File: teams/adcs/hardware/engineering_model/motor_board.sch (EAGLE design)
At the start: 63 parts

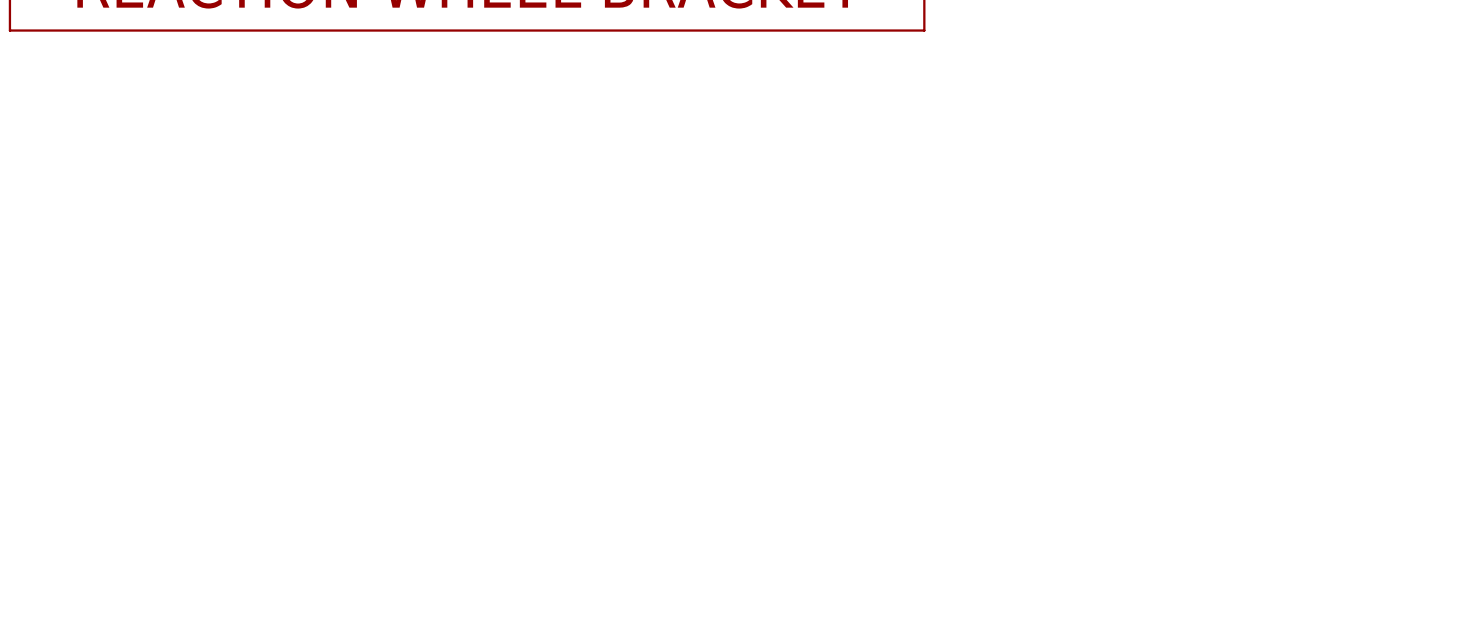
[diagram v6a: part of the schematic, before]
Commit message: ADCS/RW: Added LDOs for microcontrollers
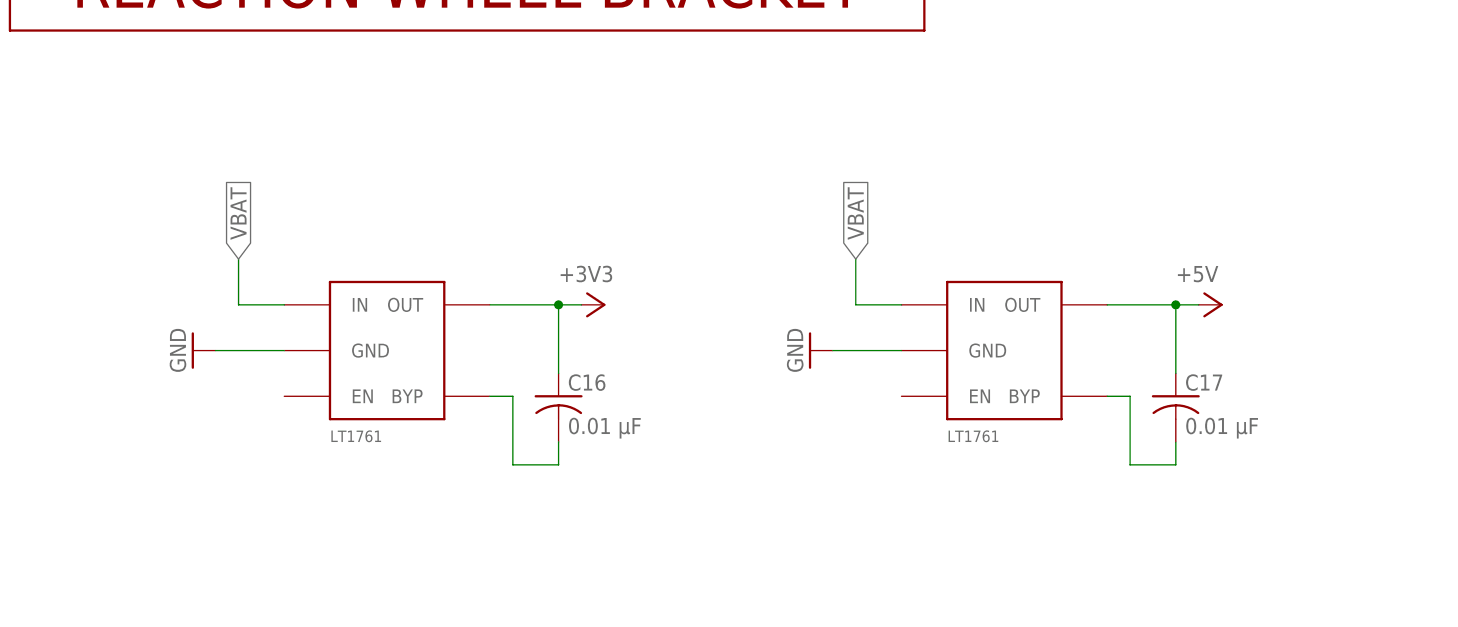
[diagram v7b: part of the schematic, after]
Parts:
- added C16, C17: 0.01 μF, rcl:C-USC0805
- added LDO_3V3, LDO_5V: LINEAR_LDO_LT1761-X, DubSat1 Components:LINEAR_LDO_LT1761-X
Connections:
- new net N$13: C17.2, LDO_5V.BYP
- new net N$14: C16.2, LDO_3V3.BYP
- net +3V3: now also C16.1, LDO_3V3.OUT
- net +5V: now also C17.1, LDO_5V.OUT
- net GND: now also LDO_3V3.GND, LDO_5V.GND
- net VBAT: now also LDO_3V3.IN, LDO_5V.IN
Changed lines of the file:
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@@
 <part name="SERIAL_X" library="SparkFun-Connectors" deviceset="CONN_03" device="LOCK"/>
 <part name="GND37" library="supply1" library_urn="urn:adsk.eagle:library:371" deviceset="GND" device=""/>
+<part name="LDO_3V3" library="DubSat1 Components" deviceset="LINEAR_LDO_LT1761-X" device=""/>
+<part name="LDO_5V" library="DubSat1 Components" deviceset="LINEAR_LDO_LT1761-X" device=""/>
+<part name="GND38" library="supply1" library_urn="urn:adsk.eagle:library:371" deviceset="GND" device=""/>
+<part name="GND39" library="supply1" library_urn="urn:adsk.eagle:library:371" deviceset="GND" device=""/>
+<part name="+3V4" library="supply1" library_urn="urn:adsk.eagle:library:371" deviceset="+3V3" device=""/>
+<part name="P+4" library="supply1" library_urn="urn:adsk.eagle:library:371" deviceset="+5V" device=""/>
+<part name="C16" library="rcl" library_urn="urn:adsk.eagle:library:334" deviceset="C-US" device="C0805" package3d_urn="urn:adsk.eagle:package:23617/2" value="0.01 μF"/>
+<part name="C17" library="rcl" library_urn="urn:adsk.eagle:library:334" deviceset="C-US" device="C0805" package3d_urn="urn:adsk.eagle:package:23617/2" value="0.01 μF"/>
 </parts>
 <sheets>
@@
 <instance part="SERIAL_X" gate="J$1" x="17.78" y="-129.54"/>
 <instance part="GND37" gate="1" x="35.56" y="-124.46" rot="R90"/>
+<instance part="LDO_3V3" gate="G$1" x="147.32" y="30.48"/>
+<instance part="LDO_5V" gate="G$1" x="215.9" y="30.48"/>
+<instance part="GND38" gate="1" x="193.04" y="30.48" rot="R270"/>
+<instance part="GND39" gate="1" x="124.46" y="30.48" rot="R270"/>
+<instance part="+3V4" gate="G$1" x="170.18" y="35.56" rot="R270"/>
+<instance part="P+4" gate="1" x="238.76" y="35.56" rot="R270"/>
+<instance part="C16" gate="G$1" x="165.1" y="25.4"/>
+<instance part="C17" gate="G$1" x="233.68" y="25.4"/>
 </instances>
 <busses>
@@
 <pinref part="GND37" gate="1" pin="GND"/>
 </segment>
+<segment>
+<pinref part="GND39" gate="1" pin="GND"/>
+<pinref part="LDO_3V3" gate="G$1" pin="GND"/>
+<wire x1="127" y1="30.48" x2="134.62" y2="30.48" width="0.1524" layer="91"/>
+</segment>
+<segment>
+<pinref part="GND38" gate="1" pin="GND"/>
+<pinref part="LDO_5V" gate="G$1" pin="GND"/>
+<wire x1="195.58" y1="30.48" x2="203.2" y2="30.48" width="0.1524" layer="91"/>
+</segment>
 </net>
 <net name="CANH" class="0">
@@
 <wire x1="38.1" y1="25.4" x2="33.02" y2="25.4" width="0.1524" layer="91"/>
 <label x="33.02" y="25.4" size="1.778" layer="95" rot="R180" xref="yes"/>
+</segment>
+<segment>
+<pinref part="LDO_3V3" gate="G$1" pin="IN"/>
+<wire x1="134.62" y1="35.56" x2="129.54" y2="35.56" width="0.1524" layer="91"/>
+<wire x1="129.54" y1="35.56" x2="129.54" y2="40.64" width="0.1524" layer="91"/>
+<label x="129.54" y="40.64" size="1.778" layer="95" rot="R90" xref="yes"/>
+</segment>
+<segment>
+<pinref part="LDO_5V" gate="G$1" pin="IN"/>
+<wire x1="203.2" y1="35.56" x2="198.12" y2="35.56" width="0.1524" layer="91"/>
+<wire x1="198.12" y1="35.56" x2="198.12" y2="40.64" width="0.1524" layer="91"/>
+<label x="198.12" y="40.64" size="1.778" layer="95" rot="R90" xref="yes"/>
 </segment>
 </net>
@@
 <junction x="261.62" y="-45.72"/>
 </segment>
+<segment>
+<pinref part="LDO_3V3" gate="G$1" pin="OUT"/>
+<pinref part="+3V4" gate="G$1" pin="+3V3"/>
+<wire x1="157.48" y1="35.56" x2="165.1" y2="35.56" width="0.1524" layer="91"/>
+<pinref part="C16" gate="G$1" pin="1"/>
+<wire x1="165.1" y1="35.56" x2="167.64" y2="35.56" width="0.1524" layer="91"/>
+<wire x1="165.1" y1="27.94" x2="165.1" y2="35.56" width="0.1524" layer="91"/>
+<junction x="165.1" y="35.56"/>
+</segment>
 </net>
 <net name="+5V" class="0">
@@
 <pinref part="P+3" gate="1" pin="+5V"/>
 <wire x1="266.7" y1="-38.1" x2="246.38" y2="-38.1" width="0.1524" layer="91"/>
+</segment>
+<segment>
+<pinref part="LDO_5V" gate="G$1" pin="OUT"/>
+<pinref part="P+4" gate="1" pin="+5V"/>
+<wire x1="226.06" y1="35.56" x2="233.68" y2="35.56" width="0.1524" layer="91"/>
+<pinref part="C17" gate="G$1" pin="1"/>
+<wire x1="233.68" y1="35.56" x2="236.22" y2="35.56" width="0.1524" layer="91"/>
+<wire x1="233.68" y1="27.94" x2="233.68" y2="35.56" width="0.1524" layer="91"/>
+<junction x="233.68" y="35.56"/>
 </segment>
 </net>
@@
 </segment>
 </net>
+<net name="N$13" class="0">
+<segment>
+<pinref part="LDO_5V" gate="G$1" pin="BYP"/>
+<wire x1="226.06" y1="25.4" x2="228.6" y2="25.4" width="0.1524" layer="91"/>
+<wire x1="228.6" y1="25.4" x2="228.6" y2="17.78" width="0.1524" layer="91"/>
+<pinref part="C17" gate="G$1" pin="2"/>
+<wire x1="228.6" y1="17.78" x2="233.68" y2="17.78" width="0.1524" layer="91"/>
+<wire x1="233.68" y1="17.78" x2="233.68" y2="20.32" width="0.1524" layer="91"/>
+</segment>
+</net>
+<net name="N$14" class="0">
+<segment>
+<pinref part="LDO_3V3" gate="G$1" pin="BYP"/>
+<wire x1="157.48" y1="25.4" x2="160.02" y2="25.4" width="0.1524" layer="91"/>
+<wire x1="160.02" y1="25.4" x2="160.02" y2="17.78" width="0.1524" layer="91"/>
+<pinref part="C16" gate="G$1" pin="2"/>
+<wire x1="160.02" y1="17.78" x2="165.1" y2="17.78" width="0.1524" layer="91"/>
+<wire x1="165.1" y1="17.78" x2="165.1" y2="20.32" width="0.1524" layer="91"/>
+</segment>
+</net>

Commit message: ADCS/RW: Routed everything but SEPIC
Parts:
- removed C10, C8: 1uF, rcl:C-USC1206
- removed C6: 2.2uF, rcl:C-USC1206
- removed C7, C9: 0.1uF, rcl:C-USC0805
- removed CMTMODY: 0_OHM_JUMPER, DubSat1 Components:0_OHM_JUMPER
- removed R10, R11, R16, R9: 3.3K, rcl:R-US_R0805
- removed R12, R13, R14: 10K, rcl:R-US_R0805
- removed R15: (no value), rcl:R-US_R0805
- removed U$5, U$8: MSP-CAN_BLOCK, DubSat1 Components:MSP-CAN_BLOCK
- removed U$6: PROGRAM/DEBUG_PORT, DubSat1 Components:PROGRAM/DEBUG_PORT
- added C18: 2.2uF, rcl:C-USC1206
- added C19, C21: 0.1uF, rcl:C-USC0805
- added C20, C22: 1uF, rcl:C-USC1206
- added CMTMOD_Y: 0_OHM_JUMPER, DubSat1 Components:0_OHM_JUMPER
- added R25, R26, R27, R32: 3.3K, rcl:R-US_R0805
- added R28, R29, R30: 10K, rcl:R-US_R0805
- added R31: (no value), rcl:R-US_R0805
- added U$12, U$15: DRV10970, DubSat1 Components:DRV10970
- added U$14: PROGRAM/DEBUG_PORT, DubSat1 Components:PROGRAM/DEBUG_PORT
- U$10, U$13: value DRV10970 -> MSP-CAN_BLOCK; device DubSat1 Components:DRV10970 -> DubSat1 Components:MSP-CAN_BLOCK
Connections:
- net N$1 renamed SBWTCK_X
- net N$2 renamed SBWTDIO_X
- net N$3 renamed TXD_X
- net N$4 renamed RXD_X
- net N$5 renamed GPIO_DEBUG_3.4_X
- net N$6 renamed GPIO_DEBUG_3.5_X
- removed net FG: U$8.P7.4_GPIO
- removed net FR: U$8.P7.3_GPIO
- removed net N$10: U$5.P2.1_RXD, U$6.P2.1_RXD
- removed net N$11: U$5.P3.4_GPIO_DEBUG, U$6.P3.4_GPIO_DEBUG
- removed net N$12: U$5.P3.5_GPIO_DEBUG, U$6.P3.5_GPIO_DEBUG
- removed net N$63: U$11.SBWTCK, U$8.SBWTCK
- removed net N$64: U$11.SBWTDIO, U$8.SBWTDIO
- removed net N$65: U$11.P2.0_TXD, U$8.P2.0_TXD
- removed net N$66: U$11.P2.1_RXD, U$8.P2.1_RXD
- removed net N$67: U$11.P3.4_GPIO_DEBUG, U$8.P3.4_GPIO_DEBUG
- removed net N$68: U$11.P3.5_GPIO_DEBUG, U$8.P3.5_GPIO_DEBUG
- removed net N$7: U$5.SBWTCK, U$6.SBWTCK
- removed net N$8: U$5.SBWTDIO, U$6.SBWTDIO
- removed net N$9: U$5.P2.0_TXD, U$6.P2.0_TXD
- removed net PWM: U$8.P1.7_GPIO/PWM
- removed net RD: U$8.P4.0_GPIO
- removed net RETRY_Z_Y: C11.1, U$13.RETRY
- removed net V1_Z: MOTOR_Z.P$2, U$10.V
- removed net VM_Z: C10.2, U$10.VM
- new net GPIO_DEBUG_3.4_Y: U$10.P3.4_GPIO_DEBUG, U$11.P3.4_GPIO_DEBUG
- new net GPIO_DEBUG_3.4_Z: U$13.P3.4_GPIO_DEBUG, U$14.P3.4_GPIO_DEBUG
- new net GPIO_DEBUG_3.5_Y: U$10.P3.5_GPIO_DEBUG, U$11.P3.5_GPIO_DEBUG
- new net GPIO_DEBUG_3.5_Z: U$13.P3.5_GPIO_DEBUG, U$14.P3.5_GPIO_DEBUG
- new net RETRY_Y: C11.1, U$12.RETRY
- new net RXD_Y: U$10.P2.1_RXD, U$11.P2.1_RXD
- new net RXD_Z: U$13.P2.1_RXD, U$14.P2.1_RXD
- new net SBWTCK_Y: U$10.SBWTCK, U$11.SBWTCK
- new net SBWTCK_Z: U$13.SBWTCK, U$14.SBWTCK
- new net SBWTDIO_Y: U$10.SBWTDIO, U$11.SBWTDIO
- new net SBWTDIO_Z: U$13.SBWTDIO, U$14.SBWTDIO
- new net TXD_Y: U$10.P2.0_TXD, U$11.P2.0_TXD
- new net TXD_Z: U$13.P2.0_TXD, U$14.P2.0_TXD
- new net V_Z: MOTOR_Z.P$2, U$15.V
- net +3V3: now also U$10.3.3V_CAN@1, U$10.3.3V_CAN@2, U$10.3.3V_MSP-ANALOG@1, U$10.3.3V_MSP@2, U$10.3.3V_MSP@3, U$13.3.3V_CAN@1, U$13.3.3V_CAN@2, U$13.3.3V_MSP-ANALOG@1, U$13.3.3V_MSP@2, U$13.3.3V_MSP@3
- net +5V: now also U$10.5V_CAN, U$13.5V_CAN
- net BRKMOD_X: now also U$3.P4.3_GPIO
- net BRKMOD_Y: now also U$10.P4.3_GPIO, U$12.BRKMOD; no longer U$13.BRKMOD
- net BRKMOD_Z: now also U$13.P4.3_GPIO, U$15.BRKMOD; no longer U$10.BRKMOD
- net CANH: now also U$10.CANH, U$13.CANH; no longer U$5.CANH, U$8.CANH
- net CANL: now also U$10.CANL, U$13.CANL; no longer U$5.CANL, U$8.CANL
- net CMTMOD_Y: now also CMTMOD_Y.SIG, U$12.CMTMOD; no longer CMTMODY.SIG, U$13.CMTMOD
- net CMTMOD_Z: now also U$15.CMTMOD; no longer U$10.CMTMOD
- net CPN_Y: now also U$12.CPN; no longer U$13.CPN
- net CPN_Z: now also C19.1, U$15.CPN; no longer C7.1, U$10.CPN
- net CPP_Y: now also U$12.CPP; no longer U$13.CPP
- net CPP_Z: now also C19.2, U$15.CPP; no longer C7.2, U$10.CPP
- net CS_Y: now also U$12.CS; no longer U$13.CS
- net CS_Z: now also R31.2, U$15.CS; no longer R15.2, U$10.CS
- net DAA_Y: now also U$12.DAA; no longer U$13.DAA
- net DAA_Z: now also U$15.DAA; no longer U$10.DAA
- net FG_Y: now also U$10.P7.4_GPIO, U$12.FG; no longer U$13.FG, U$5.P7.4_GPIO
- net FG_Z: now also R32.2, U$13.P7.4_GPIO, U$15.FG; no longer R16.2, U$10.FG
- net FR_Y: now also U$10.P7.3_GPIO, U$12.FR; no longer U$13.FR, U$5.P7.3_GPIO
- net FR_Z: now also U$13.P7.3_GPIO, U$15.FR; no longer U$10.FR
- net GND: now also C18.2, C20.1, C21.1, C22.1, CMTMOD_Y.GND, R26.1, R31.1, U$12.GND, U$14.GND@1, U$14.GND@2, U$15.GND; no longer C10.1, C6.2, C8.1, C9.1, CMTMODY.GND, R10.1, R15.1, U$5.GND, U$6.GND@1, U$6.GND@2, U$8.GND
- net HN_Y: now also U$12.U_HN, U$12.V_HN, U$12.W_HN; no longer U$13.U_HN, U$13.V_HN, U$13.W_HN
- net HN_Z: now also R26.2, R27.1, U$15.U_HN, U$15.V_HN, U$15.W_HN; no longer R10.2, R11.1, U$10.U_HN, U$10.V_HN, U$10.W_HN
- net HP_U_Y: now also U$12.U_HP; no longer U$13.U_HP
- net HP_U_Z: now also R28.2, U$15.U_HP; no longer R12.2, U$10.U_HP
- net HP_V_Y: now also U$12.V_HP; no longer U$13.V_HP
- net HP_V_Z: now also R29.2, U$15.V_HP; no longer R13.2, U$10.V_HP
- net HP_W_Y: now also U$12.W_HP; no longer U$13.W_HP
- net HP_W_Z: now also R30.2, U$15.W_HP; no longer R14.2, U$10.W_HP
- net M_Y_RX: now also U$10.P2.6_GPIO/PWM; no longer U$5.P2.6_GPIO/PWM
- net M_Y_TX: now also U$10.P2.5_GPIO; no longer U$5.P2.5_GPIO
- net M_Z_RX: now also U$13.P2.6_GPIO/PWM; no longer U$8.P2.6_GPIO/PWM
- net M_Z_TX: now also U$13.P2.5_GPIO; no longer U$8.P2.5_GPIO
- net PWM_Y: now also U$10.P1.7_GPIO/PWM, U$12.PWM; no longer U$13.PWM, U$5.P1.7_GPIO/PWM
- net PWM_Z: now also U$13.P1.7_GPIO/PWM, U$15.PWM; no longer U$10.PWM
- net RD_Y: now also U$10.P4.0_GPIO, U$12.RD; no longer U$13.RD, U$5.P4.0_GPIO
- net RD_Z: now also R25.1, U$13.P4.0_GPIO, U$15.RD; no longer R9.1, U$10.RD
- net RETRY_Z: now also C18.1, U$15.RETRY; no longer C6.1, U$10.RETRY
- net SYNC1: now also U$10.P7.2_SYNC1, U$13.P7.2_SYNC1; no longer U$5.P7.2_SYNC1, U$8.P7.2_SYNC1
- net SYNC2: now also U$10.PJ.3_SYNC2, U$13.PJ.3_SYNC2; no longer U$5.PJ.3_SYNC2, U$8.PJ.3_SYNC2
- net U_Y: now also U$12.U; no longer U$13.U
- net U_Z: now also U$15.U; no longer U$10.U
- net VCP_Y: now also U$12.VCP; no longer U$13.VCP
- net VCP_Z: now also C20.2, U$15.VCP; no longer C8.2, U$10.VCP
- net VINT_Y: now also CMTMOD_Y.VCC, U$12.VINT; no longer CMTMODY.VCC, U$13.VINT
- net VINT_Z: now also C21.2, R25.2, R27.2, R28.1, R29.1, R30.1, R32.1, U$15.VINT; no longer C9.2, R11.2, R12.1, R13.1, R14.1, R16.1, R9.2, U$10.VINT
- net VM: now also C22.2, U$12.VM, U$15.VM; no longer U$13.VM
- net V_Y: now also U$12.V; no longer U$13.V
- net W_Y: now also U$12.W; no longer U$13.W
- net W_Z: now also U$15.W; no longer U$10.W
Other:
- moved on the sheet: C1, C11, C12, C13, C14, C15, C2, C3, C4, C5, CMTMOD_X, CMTMOD_Z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
